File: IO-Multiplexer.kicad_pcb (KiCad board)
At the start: 2 copper layers, 68.6 x 129.5 mm, 19 parts

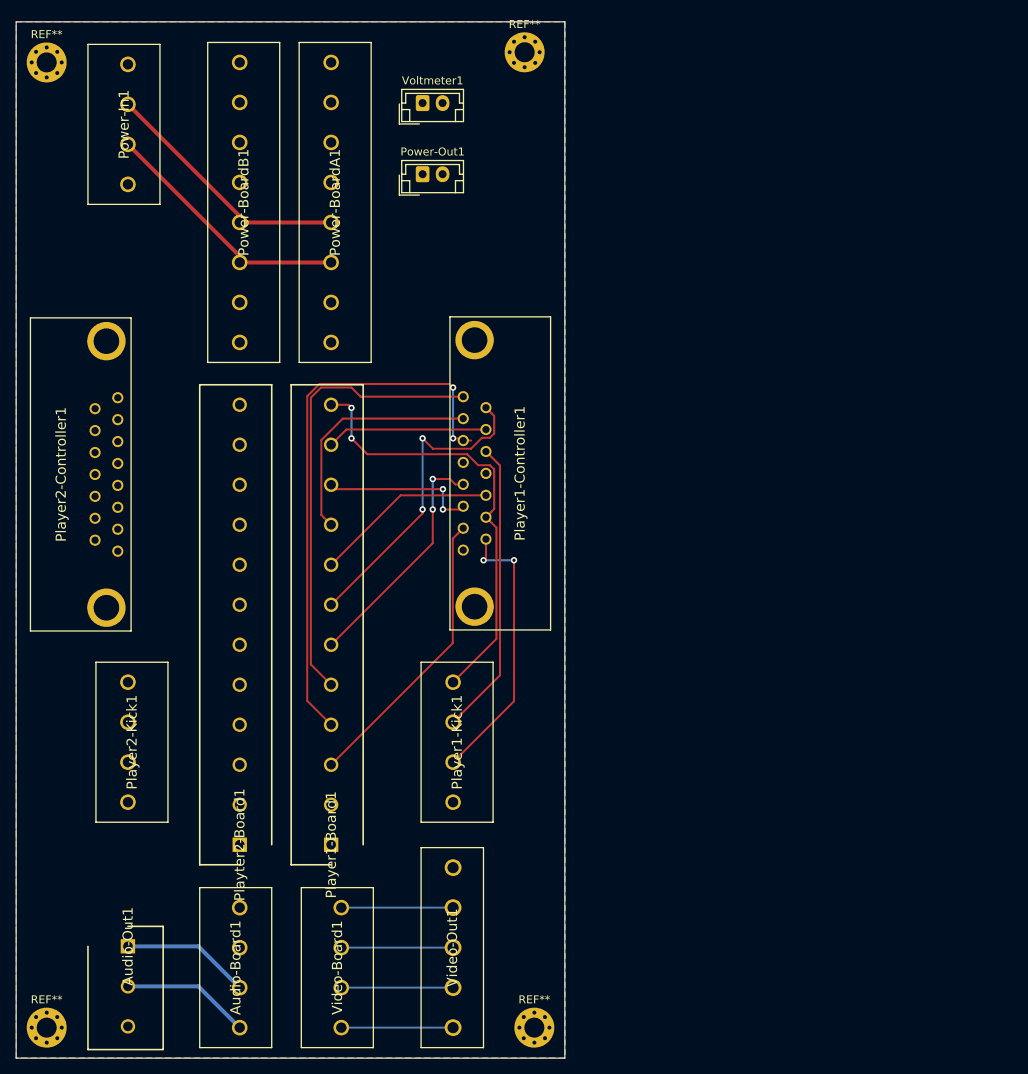
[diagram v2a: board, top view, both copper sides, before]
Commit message: Rerouted all controls
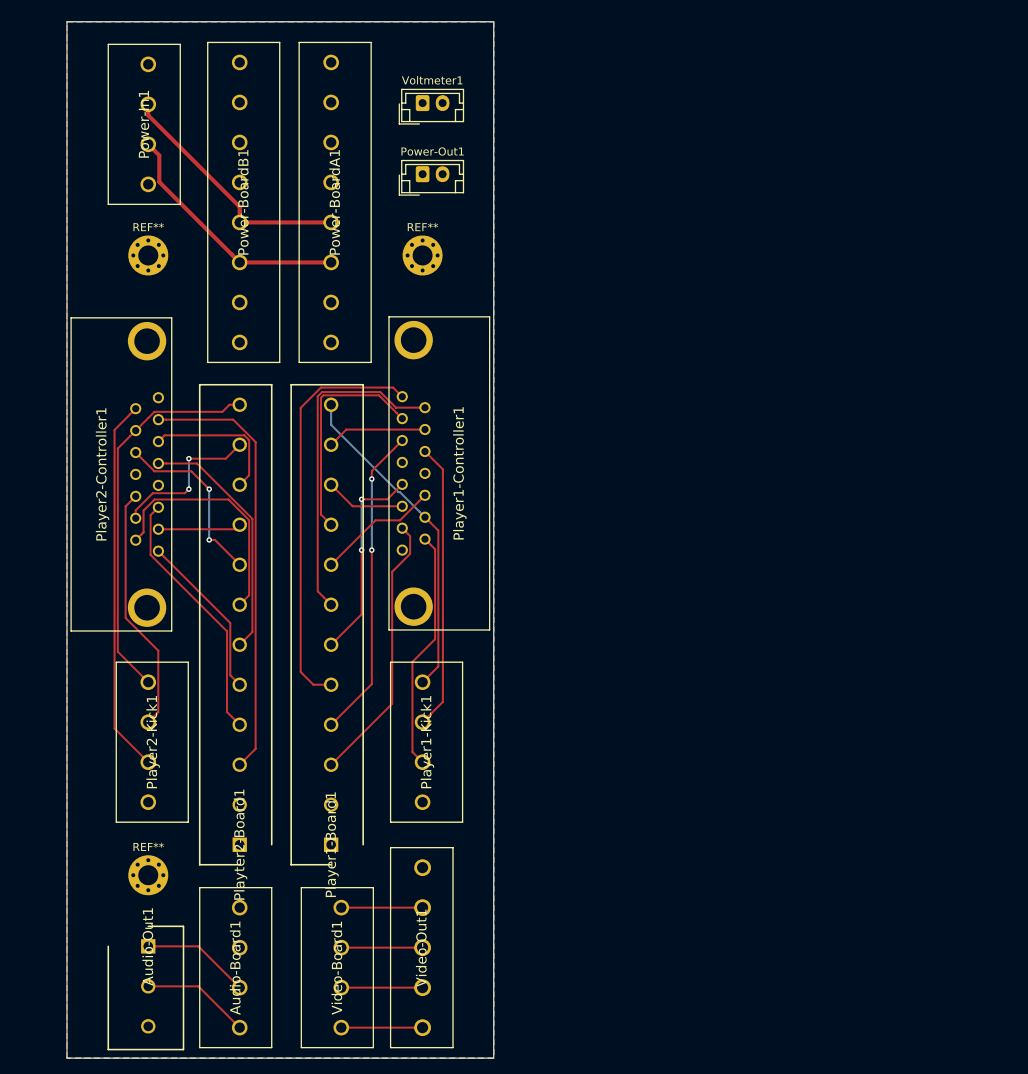
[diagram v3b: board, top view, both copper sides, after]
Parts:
- removed the REF** at (203.2, 139.7)
- removed the REF** at (142.2, 139.7)
- added REF**: MountingHole_2.5mm_Pad_Via, MountingHole:MountingHole_2.5mm_Pad_Via, F.Cu at (154.9, 120.7)
- moved REF** 28.4 mm to (189.2, 43.2)
- moved REF** 27.3 mm to (154.9, 43.2)
- moved Player1-Controller1 7.62 mm to (186.7, 80.0)
- moved Player2-Controller1 5.08 mm to (156.2, 61.0)
- moved Player1-Kick1 3.81 mm to (189.2, 96.5)
- moved Video-Out1 3.81 mm to (189.2, 139.7)
- moved Audio-Out1 2.54 mm to (154.9, 129.5)
- moved Player2-Kick1 2.54 mm to (154.9, 96.5)
- moved Power-In1 2.54 mm to (154.9, 34.3)
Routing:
- net /P2-Coin: track 0.00 -> 54.5 mm
- net /P2-Button4: track 0.00 -> 48.3 mm
- net /P2-Button6: track 0.00 -> 47.0 mm
- net /P2-Start: track 0.00 -> 32.2 mm
- net /P2-Down: track 0.00 -> 31.0 mm
- net /P2-Button5: track 0.00 -> 31.0 mm
- net /P1-Start: track 70.1 -> 39.2 mm
- net /P2-Left: track 0.00 -> 30.0 mm
- net /P2-Right: track 0.00 -> 22.5 mm, vias 0 -> 2
- net /P2-Up: track 0.00 -> 20.9 mm
- net /P2-Button3: track 0.00 -> 19.6 mm, vias 0 -> 2
- net /P2-Button2: track 0.00 -> 18.0 mm
- net /P1-Button4: track 55.8 -> 41.1 mm, vias 2 -> 0
- net /P2-Button1: track 0.00 -> 10.4 mm
- net /P1-Button2: track 19.4 -> 10.0 mm, vias 2 -> 0
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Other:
- board size 68.6 x 129.5 mm -> 53.3 x 129.5 mm
- net class Default: clearance 0.2 -> 0.1524; trace_width 0.25 -> 0.1524; via_dia 0.8 -> 0.6858; via_drill 0.4 -> 0.3302
- rule pad_to_mask_clearance: 0.051 -> 0.0508
- rule solder_mask_min_width: 0.25 -> 0.1016
- rule trace_clearance: 0.2 -> 0.1524
- rule trace_min: 0.2 -> 0.1524
- rule via_min_drill: 0.3 -> 0.254
- rule via_min_size: 0.4 -> 0.508

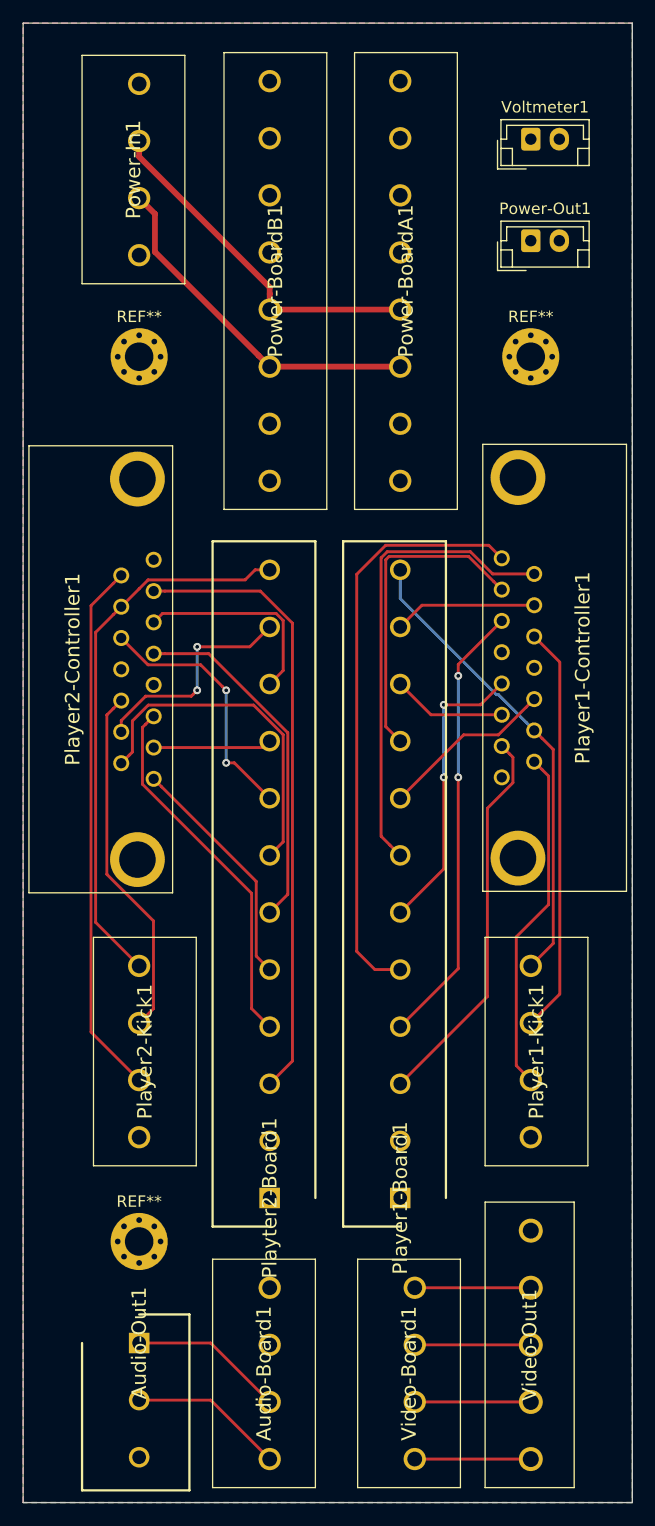
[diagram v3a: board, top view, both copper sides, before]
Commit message: add b.silk text
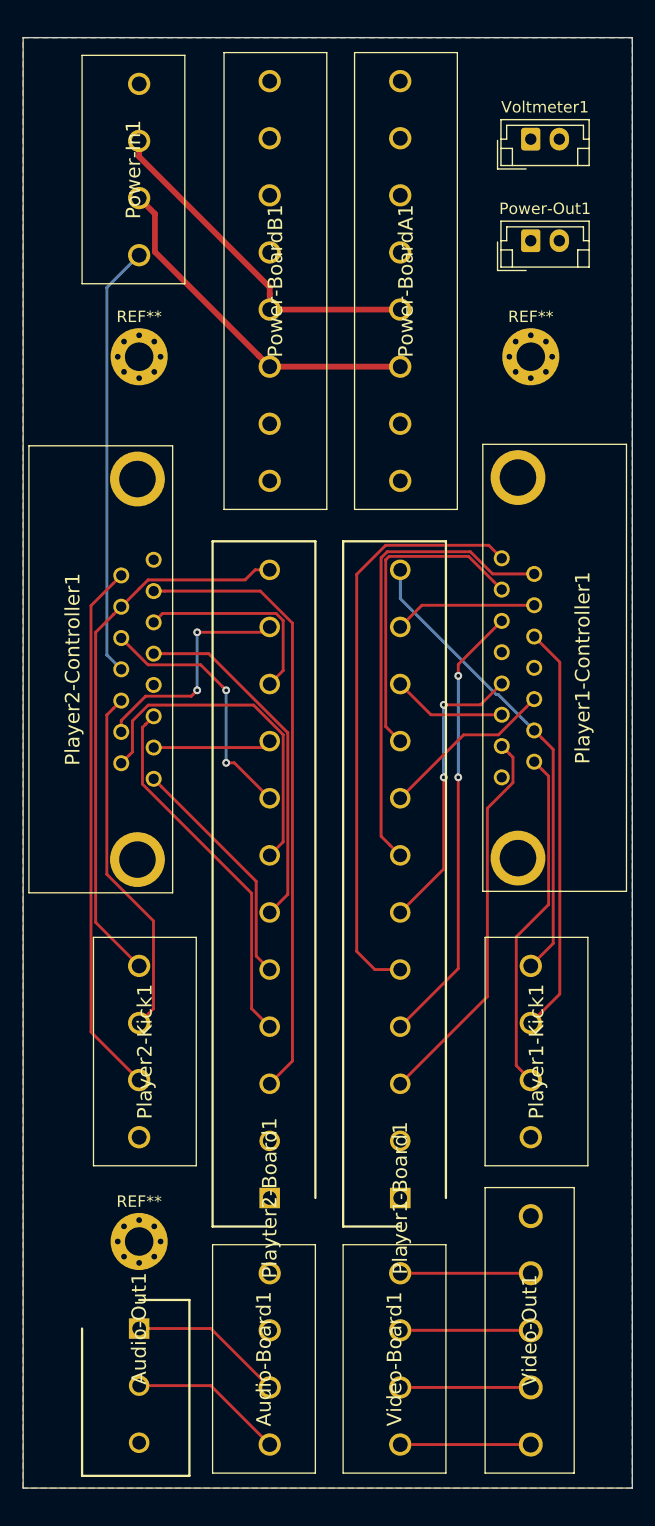
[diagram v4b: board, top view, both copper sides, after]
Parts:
- moved Video-Board1 1.80 mm to (177.8, 138.4)
- moved Audio-Board1 1.27 mm to (166.4, 138.4)
- moved Audio-Out1 1.27 mm to (154.9, 128.3)
- moved Video-Out1 1.27 mm to (189.2, 138.4)
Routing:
- net /+5V: track 0.00 -> 38.0 mm
- net /Sync: track 10.2 -> 11.4 mm
- net /Red: track 10.2 -> 11.4 mm
- net /Green: track 10.2 -> 11.4 mm
- net /Blue: track 10.2 -> 11.4 mm
- net /P2-Button3: track 19.6 -> 20.4 mm
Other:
- board size 53.3 x 129.5 mm -> 53.3 x 127 mm
- board text added: "I/O Multiplexer V0.1 anders@conbere.org"
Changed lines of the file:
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@@
   (general
     (thickness 1.6)
-    (drawings 4)
-    (tracks 156)
+    (drawings 5)
+    (tracks 160)
     (zones 0)
     (modules 18)
@@
   )
   (module SamacSys:TB003500P05BE (layer F.Cu)
-    (at 189.23 139.7 90)
+    (at 189.23 138.43 90)
     (descr TB003-500-P05BE-2)
     (tags Connector)
@@
   )
   (module SamacSys:TB00150004BE (layer F.Cu)
-    (at 179.07 139.7 90)
+    (at 177.8 138.43 90)
     (descr TB001-500-04BE-3)
     (tags Connector)
@@
   )
   (module SamacSys:TB00150004BE (layer F.Cu)
-    (at 166.37 139.7 90)
+    (at 166.37 138.43 90)
     (descr TB001-500-04BE-3)
     (tags Connector)
@@
   )
   (module SamacSys:SHDR3W100P0X500_1X3_1500X900X1290P (layer F.Cu)
-    (at 154.94 129.54 270)
+    (at 154.94 128.27 270)
     (descr TB001-500-03BE)
     (tags Connector)
@@
     )
   )
-  (gr_line (start 144.78 143.51) (end 144.78 13.97) (layer Edge.Cuts) (width 0.05))
-  (gr_line (start 198.12 143.51) (end 144.78 143.51) (layer Edge.Cuts) (width 0.05))
-  (gr_line (start 198.12 13.97) (end 198.12 143.51) (layer Edge.Cuts) (width 0.05))
-  (gr_line (start 144.78 13.97) (end 198.12 13.97) (layer Edge.Cuts) (width 0.05))
-  (segment (start 179.07 139.7) (end 189.23 139.7) (width 0.254) (layer F.Cu) (net 1))
-  (segment (start 179.07 134.7) (end 189.23 134.7) (width 0.254) (layer F.Cu) (net 2))
-  (segment (start 179.07 129.7) (end 189.23 129.7) (width 0.254) (layer F.Cu) (net 3))
-  (segment (start 179.07 124.7) (end 189.23 124.7) (width 0.254) (layer F.Cu) (net 4))
+  (gr_text "I/O Multiplexer V0.1\nanders@conbere.org" (at 171.45 90.17 90) (layer B.SilkS)
+    (effects (font (size 1 1) (thickness 0.15)) (justify mirror))
+  )
+  (gr_line (start 144.78 142.24) (end 144.78 15.24) (layer Edge.Cuts) (width 0.05))
+  (gr_line (start 198.12 142.24) (end 144.78 142.24) (layer Edge.Cuts) (width 0.05))
+  (gr_line (start 198.12 15.24) (end 198.12 142.24) (layer Edge.Cuts) (width 0.05))
+  (gr_line (start 144.78 15.24) (end 198.12 15.24) (layer Edge.Cuts) (width 0.05))
+  (segment (start 177.8 138.43) (end 189.23 138.43) (width 0.254) (layer F.Cu) (net 1))
+  (segment (start 177.8 133.43) (end 189.23 133.43) (width 0.254) (layer F.Cu) (net 2))
+  (segment (start 177.8 128.43) (end 189.23 128.43) (width 0.254) (layer F.Cu) (net 3))
+  (segment (start 177.8 123.43) (end 189.23 123.43) (width 0.254) (layer F.Cu) (net 4))
+  (segment (start 161.21 133.27) (end 166.37 138.43) (width 0.254) (layer F.Cu) (net 7))
+  (segment (start 154.94 133.27) (end 161.21 133.27) (width 0.254) (layer F.Cu) (net 7))
+  (segment (start 161.21 128.27) (end 166.37 133.43) (width 0.254) (layer F.Cu) (net 8))
+  (segment (start 154.94 128.27) (end 161.21 128.27) (width 0.254) (layer F.Cu) (net 8))
   (via (at 160.02 72.39) (size 0.6858) (drill 0.3302) (layers F.Cu B.Cu) (net 27))
-  (via (at 160.02 68.58) (size 0.6858) (drill 0.3302) (layers F.Cu B.Cu) (net 27))
-  (segment (start 161.21 134.54) (end 166.37 139.7) (width 0.254) (layer F.Cu) (net 7))
-  (segment (start 154.94 134.54) (end 161.21 134.54) (width 0.254) (layer F.Cu) (net 7))
-  (segment (start 161.21 129.54) (end 166.37 134.7) (width 0.254) (layer F.Cu) (net 8))
-  (segment (start 154.94 129.54) (end 161.21 129.54) (width 0.254) (layer F.Cu) (net 8))
+  (via (at 160.02 67.31) (size 0.6858) (drill 0.3302) (layers F.Cu B.Cu) (net 27))
+  (segment (start 153.965001 35.264999) (end 154.94 34.29) (width 0.254) (layer B.Cu) (net 9))
+  (segment (start 152.110599 37.119401) (end 153.965001 35.264999) (width 0.254) (layer B.Cu) (net 9))
+  (segment (start 152.110599 69.290599) (end 152.110599 37.119401) (width 0.254) (layer B.Cu) (net 9))
+  (segment (start 153.37 70.55) (end 152.110599 69.290599) (width 0.254) (layer B.Cu) (net 9))
   (via (at 162.56 72.39) (size 0.6858) (drill 0.3302) (layers F.Cu B.Cu) (net 32))
   (via (at 162.56 78.74) (size 0.6858) (drill 0.3302) (layers F.Cu B.Cu) (net 32))
@@
   (segment (start 153.37 75.040051) (end 155.51065 72.899401) (width 0.254) (layer F.Cu) (net 27))
   (segment (start 153.37 76.03) (end 153.37 75.040051) (width 0.254) (layer F.Cu) (net 27))
-  (segment (start 164.63 68.58) (end 166.37 66.84) (width 0.254) (layer F.Cu) (net 27))
-  (segment (start 160.02 68.58) (end 164.63 68.58) (width 0.254) (layer F.Cu) (net 27))
-  (segment (start 160.02 68.58) (end 160.02 72.39) (width 0.254) (layer B.Cu) (net 27))
+  (segment (start 160.02 67.31) (end 160.02 72.39) (width 0.254) (layer B.Cu) (net 27))
+  (segment (start 165.9 67.31) (end 166.37 66.84) (width 0.254) (layer F.Cu) (net 27))
+  (segment (start 160.02 67.31) (end 165.9 67.31) (width 0.254) (layer F.Cu) (net 27))
   (segment (start 155.510001 75.359999) (end 156.21 74.66) (width 0.254) (layer F.Cu) (net 28))
   (segment (start 155.230599 75.639401) (end 155.510001 75.359999) (width 0.254) (layer F.Cu) (net 28))
@@
     (polygon
       (pts
-        (xy 198.12 143.51) (xy 144.78 143.51) (xy 144.78 13.97) (xy 198.12 13.97)
+        (xy 198.12 142.24) (xy 144.78 142.24) (xy 144.78 15.24) (xy 198.12 15.24)
       )
     )
@@
     (polygon
       (pts
-        (xy 198.12 143.51) (xy 144.78 143.51) (xy 144.78 13.97) (xy 198.12 13.97)
+        (xy 198.12 142.24) (xy 144.78 142.24) (xy 144.78 15.24) (xy 198.12 15.24)
       )
     )
